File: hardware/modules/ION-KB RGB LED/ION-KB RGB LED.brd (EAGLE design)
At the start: 9.1 x 2.3 mm, 3 parts

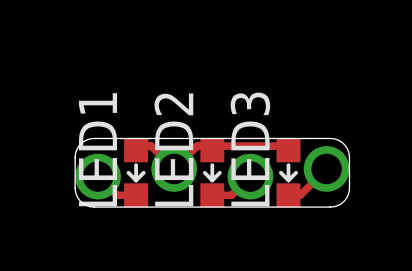
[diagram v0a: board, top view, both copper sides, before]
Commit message: Switch to single RGB LED
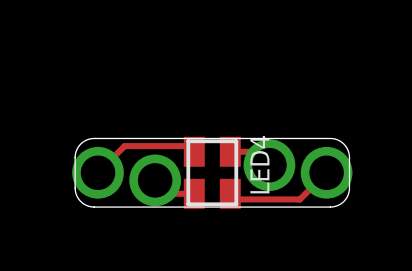
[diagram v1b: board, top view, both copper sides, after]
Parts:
- removed LED1: Red, Jordi:L0603
- removed LED2: Green, Jordi:L0603
- removed LED3: Blue, Jordi:L0603
- added LED4: LED-RGB-CASMD, Jordi:LED-SMD-RGB
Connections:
- net A: now also LED4.A; no longer LED1.A, LED2.A, LED3.A
- net B: now also LED4.B; no longer LED3.C
- net G: now also LED4.G; no longer LED2.C
- net R: now also LED4.R; no longer LED1.C
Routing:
- net A: track 6.13 -> 1.49 mm
- net G: track 1.53 -> 3.66 mm
- net B: track 1.63 -> 3.66 mm
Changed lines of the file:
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@@
 <setting verticaltext="up"/>
 </settings>
-<grid distance="5" unitdist="mil" unit="mil" style="lines" multiple="1" display="yes" altdistance="0.025" altunitdist="inch" altunit="inch"/>
+<grid distance="10" unitdist="mil" unit="mil" style="lines" multiple="1" display="yes" altdistance="0.025" altunitdist="inch" altunit="inch"/>
 <layers>
 <layer number="1" name="Top" color="4" fill="1" visible="yes" active="yes"/>
@@
 <layer number="43" name="vRestrict" color="2" fill="10" visible="yes" active="yes"/>
 <layer number="44" name="Drills" color="7" fill="1" visible="no" active="yes"/>
-<layer number="45" name="Holes" color="7" fill="1" visible="no" active="yes"/>
+<layer number="45" name="Holes" color="7" fill="1" visible="yes" active="yes"/>
 <layer number="46" name="Milling" color="3" fill="1" visible="no" active="yes"/>
 <layer number="47" name="Measures" color="7" fill="1" visible="no" active="yes"/>
@@
 </autorouter>
 <elements>
-<element name="LED1" library="Jordi" package="L0603" value="Red" x="2.032" y="1.143" rot="R90"/>
-<element name="LED2" library="Jordi" package="L0603" value="Green" x="4.572" y="1.143" rot="R90"/>
-<element name="LED3" library="Jordi" package="L0603" value="Blue" x="7.112" y="1.143" rot="R90"/>
+<element name="LED4" library="Jordi" package="LED-SMD-RGB" value="LED-RGB-CASMD" x="4.572" y="1.143" rot="R270"/>
 </elements>
 <signals>
 <signal name="A">
-<contactref element="LED1" pad="A"/>
-<contactref element="LED2" pad="A"/>
-<contactref element="LED3" pad="A"/>
-<via x="3.302" y="1.27" extent="1-16" drill="1.016" diameter="1.27"/>
-<wire x1="2.54" y1="2.032" x2="3.302" y2="1.27" width="0.254" layer="1"/>
-<wire x1="4.064" y1="2.032" x2="3.302" y2="1.27" width="0.254" layer="1"/>
-<wire x1="7.112" y1="1.893" x2="7.112" y2="2.032" width="0.254" layer="1"/>
-<wire x1="7.112" y1="2.032" x2="4.572" y2="2.032" width="0.254" layer="1"/>
-<wire x1="2.032" y1="1.893" x2="2.032" y2="2.032" width="0.254" layer="1"/>
-<wire x1="2.032" y1="2.032" x2="2.54" y2="2.032" width="0.254" layer="1"/>
-<wire x1="4.064" y1="2.032" x2="4.572" y2="2.032" width="0.254" layer="1"/>
-<wire x1="4.572" y1="2.032" x2="4.572" y2="1.893" width="0.254" layer="1"/>
+<via x="2.667" y="0.889" extent="1-16" drill="1.15" diameter="1.27"/>
+<contactref element="LED4" pad="A"/>
+<wire x1="2.667" y1="0.889" x2="3.113" y2="0.443" width="0.2032" layer="1"/>
+<wire x1="3.113" y1="0.443" x2="3.972" y2="0.443" width="0.2032" layer="1"/>
 </signal>
 <signal name="R">
-<contactref element="LED1" pad="C"/>
-<via x="0.762" y="1.016" extent="1-16" drill="1.016" diameter="1.27"/>
-<wire x1="2.032" y1="0.393" x2="1.385" y2="0.393" width="0.254" layer="1"/>
-<wire x1="1.385" y1="0.393" x2="0.762" y2="1.016" width="0.254" layer="1"/>
+<via x="6.477" y="1.397" extent="1-16" drill="1.15" diameter="1.27"/>
+<contactref element="LED4" pad="R"/>
+<wire x1="6.477" y1="1.397" x2="6.031" y2="1.843" width="0.2032" layer="1"/>
+<wire x1="6.031" y1="1.843" x2="5.172" y2="1.843" width="0.2032" layer="1"/>
 </signal>
 <signal name="G">
-<contactref element="LED2" pad="C"/>
-<via x="5.842" y="1.016" extent="1-16" drill="1.016" diameter="1.27"/>
-<wire x1="4.572" y1="0.393" x2="5.219" y2="0.393" width="0.254" layer="1"/>
-<wire x1="5.219" y1="0.393" x2="5.842" y2="1.016" width="0.254" layer="1"/>
+<via x="0.762" y="1.143" extent="1-16" drill="1.15" diameter="1.27"/>
+<contactref element="LED4" pad="G"/>
+<wire x1="3.972" y1="1.843" x2="3.783" y2="2.032" width="0.2032" layer="1"/>
+<wire x1="3.783" y1="2.032" x2="1.651" y2="2.032" width="0.2032" layer="1"/>
+<wire x1="0.762" y1="1.143" x2="1.651" y2="2.032" width="0.2032" layer="1"/>
 </signal>
 <signal name="B">
-<contactref element="LED3" pad="C"/>
-<via x="8.382" y="1.27" extent="1-16" drill="1.016" diameter="1.27"/>
-<wire x1="7.112" y1="0.393" x2="7.505" y2="0.393" width="0.254" layer="1"/>
-<wire x1="7.505" y1="0.393" x2="8.382" y2="1.27" width="0.254" layer="1"/>
+<via x="8.382" y="1.143" extent="1-16" drill="1.15" diameter="1.27"/>
+<contactref element="LED4" pad="B"/>
+<wire x1="5.172" y1="0.443" x2="5.361" y2="0.254" width="0.2032" layer="1"/>
+<wire x1="5.361" y1="0.254" x2="7.493" y2="0.254" width="0.2032" layer="1"/>
+<wire x1="8.382" y1="1.143" x2="7.493" y2="0.254" width="0.2032" layer="1"/>
 </signal>
 </signals>
